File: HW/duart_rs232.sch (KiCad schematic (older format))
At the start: 12 parts, among them J6 RS232a, J7 RS232b, U22 MAX238, U23 SC28L92PLCC44, X2 3.6864MHz

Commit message: Disable power down. Align init code to force a page break when reading the init table.
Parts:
- X2: symbol Oscillator:SG-8002CA -> pluto-rescue:SG-8002CA-Oscillator
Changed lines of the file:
@@
 EESchema Schematic File Version 4
-LIBS:pluto-cache
 EELAYER 30 0
 EELAYER END
@@
 DUART ($7FE0)
 $Comp
-L Oscillator:SG-8002CA X2
+L pluto-rescue:SG-8002CA-Oscillator X2
 U 1 1 5D6A4602
 P 9675 4875
+AR Path="/5D6A4602" Ref="X2"  Part="1"
+AR Path="/59ECC1E1/5D6A4602" Ref="X2"  Part="1"
 F 0 "X2" H 9525 5125 50  0000 L CNN
 F 1 "3.6864MHz" H 9250 4625 50  0000 L CNN

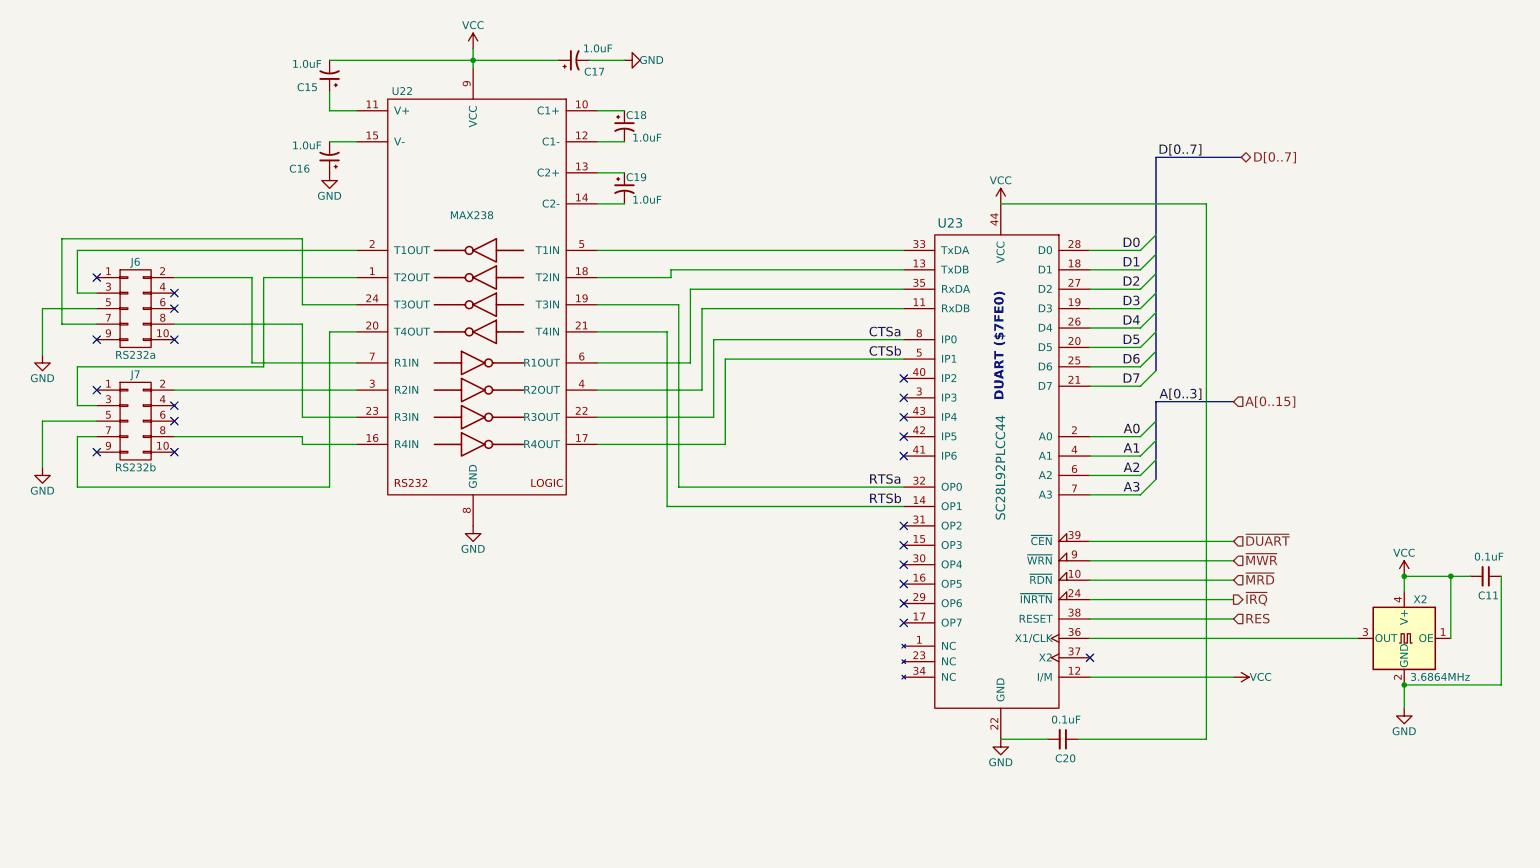
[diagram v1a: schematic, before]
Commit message: New version with a TL16C550 UART
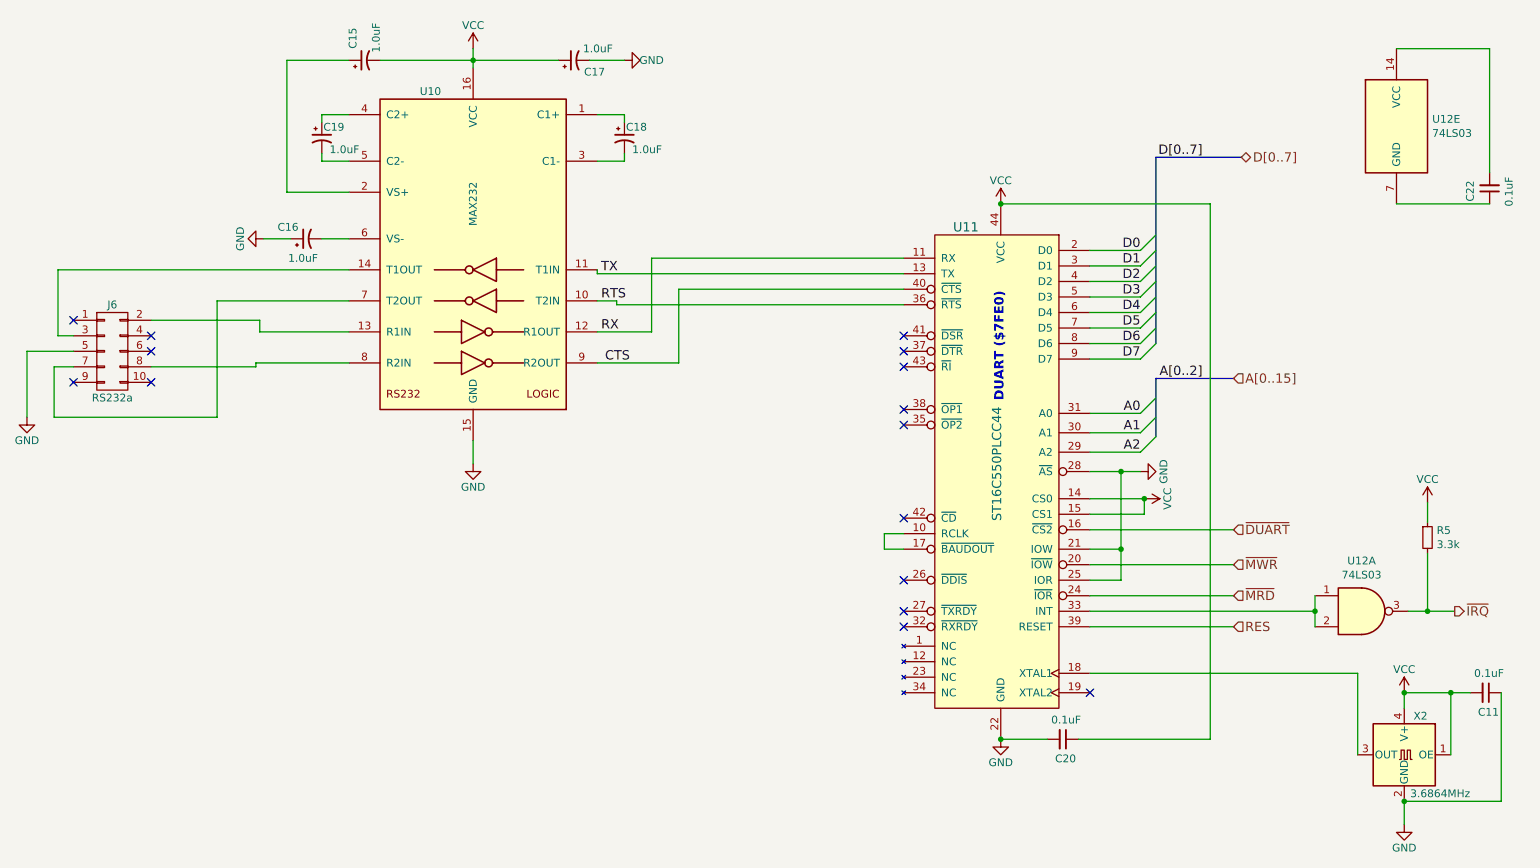
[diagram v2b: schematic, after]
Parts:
- removed J7: RS232b, Connector_IDC:IDC-Header_2x05_P2.54mm_Vertical, symbol pluto-rescue:CONN_02X05-conn
- removed U22: MAX238, Package_SO:SOIC-24W_7.5x15.4mm_P1.27mm, symbol pluto:MAX238
- removed U23: SC28L92PLCC44, Package_LCC:PLCC-44_THT-Socket, symbol pluto:SC28L92PLCC44
- added C22: 0.1uF, Capacitor_SMD:C_0805_2012Metric_Pad1.15x1.40mm_HandSolder, symbol pluto-rescue:C_Small-device
- added R5: 3.3k, Resistor_SMD:R_1206_3216Metric_Pad1.42x1.75mm_HandSolder, symbol Device:R_Small
- added U10: MAX232, Package_SO:SOIC-16W_7.5x10.3mm_P1.27mm, symbol Interface_UART:MAX232
- added U11: ST16C550PLCC44, Package_LCC:PLCC-44_THT-Socket, symbol grotto:ST16C550PLCC44
- added U12: 74LS03, Package_SO:SOIC-14_3.9x8.7mm_P1.27mm, symbol 74xx:74LS03
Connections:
- net A0: now also U11.31 (A0)
- net A1: now also U11.30 (A1)
- net A2: now also U11.29 (A2)
- net D0: now also U11.2 (D0)
- net D1: now also U11.3 (D1)
- net D2: now also U11.4 (D2)
- net D3: now also U11.5 (D3)
- net D4: now also U11.6 (D4)
- net D5: now also U11.7 (D5)
- net D6: now also U11.8 (D6)
- net D7: now also U11.9 (D7)
- net GND: now also U10.15 (GND), U11.21 (IOW), U11.22 (GND), U11.25 (IOR), U11.28 (~AS)
- net RES: now also U11.39 (RESET)
- net VCC: now also R5.1, U10.16 (VCC), U11.14 (CS0), U11.15 (CS1), U11.44 (VCC)
- net ~DUART: now also U11.16 (~CS2)
- net ~IRQ: now also R5.2, U12.3
- net ~MRD: now also U11.24 (~IOR)
- net ~MWR: now also U11.20 (~IOW)
- net at C18.1: now also U10.1 (C1+)
- net at C15.1: now also U10.2 (VS+)
- net at C18.2: now also U10.3 (C1-)
- net at C19.1: now also U10.4 (C2+)
- net at C19.2: now also U10.5 (C2-)
- net at C16.2: now also U10.6 (VS-)
- net at J6.3 (P3): now also U10.14 (T1OUT)
- net at J6.8 (P8): now also U10.8 (R2IN)
- net at J6.7 (P7): now also U10.7 (T2OUT)
- net at J6.2 (P2): now also U10.13 (R1IN)
- net at X2.3 (OUT): now also U11.18 (XTAL1)
- new net: U11.10 (RCLK), U11.17 (~BAUDOUT)
- new net: U11.33 (INT), U12.1, U12.2
- new net: C22.2, U12.14 (VCC)
- new net: C22.1, U12.7 (GND)
- new net CTS: U10.9 (R2OUT), U11.40 (~CTS)
- new net RTS: U10.10 (T2IN), U11.36 (~RTS)
- new net RX: U10.12 (R1OUT), U11.11 (RX)
- new net TX: U10.11 (T1IN), U11.13 (TX)
- no-connect marks 22 -> 15
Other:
- moved on the sheet: C11, C15, C16, C18, C19, X2

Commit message: small updates
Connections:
- net GND: now also C22.1, U12.7 (GND)
- net VCC: now also C22.2, U12.14 (VCC)
- net UART_CLK: now reaches U11.18 (XTAL1), X2.3 (OUT)
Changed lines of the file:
@@
 Wire Bus Line
 	8075 1775 8075 2975
+$Comp
+L power:VCC #PWR0104
+U 1 1 61105D72
+P 9625 1075
+F 0 "#PWR0104" H 9625 925 50  0001 C CNN
+F 1 "VCC" H 9640 1248 50  0000 C CNN
+F 2 "" H 9625 1075 50  0001 C CNN
+F 3 "" H 9625 1075 50  0001 C CNN
+	1    9625 1075
+	1    0    0    -1
+$EndComp
+Connection ~ 9625 1075
+$Comp
+L power:GND #PWR0105
+U 1 1 6110623B
+P 9625 2075
+F 0 "#PWR0105" H 9625 1825 50  0001 C CNN
+F 1 "GND" H 9630 1902 50  0000 C CNN
+F 2 "" H 9625 2075 50  0001 C CNN
+F 3 "" H 9625 2075 50  0001 C CNN
+	1    9625 2075
+	1    0    0    -1
+$EndComp
+Connection ~ 9625 2075
+Text Label 9375 5100 2    60   ~ 0
+UART_CLK
 $EndSCHEMATC
